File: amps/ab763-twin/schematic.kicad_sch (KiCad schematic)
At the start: 130 parts, among them T1 125P34A · 340-0-340 V, T2 125C1A, T3 125A29A, T4 125A20B

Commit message: Fix: schematic sheets — real title block, fitted paper, no lettering through circuitry
Every sheet in the corpus shipped with an EMPTY title block ("Title:" and
"Date:" blank, default "Sheet /" furniture) laid onto a fixed A4/A3 page
regardless of the drawing's size, with prose annotations placed by hand
wherever a coordinate looked free when the amp was first drawn. The result
read as an unfinished alpha under a `verified` badge: KiCanvas's default view
is `zoom_to_page()`, so a 150 x 110 mm circuit on an A3 sheet opened as a
postage stamp, and later edits had pushed live circuitry under the prose.

schematic_lib.py — the builder now records each element as a (kind, points,
extra) tuple instead of a finished string, so `write()` can measure and move
what it emits:

- emits a real `(title_block …)` read from the amp's own meta.yaml — Title =
  designation + style, Date = the verification (or added) date, Rev = the
  verification status, Company = Circuit Codex, plus the licence and source
  URL as comments. Fixes all 34 sheets from one place;
- emits `(paper "User" w h)` cut to the drawing, translated to a fixed margin,
  with the bottom 34 mm strip reserved for the worksheet's title block. Sheet
  utilisation of the drawable area went from as low as ~20% to 92-98%;
- `note()` queues prose into a wrapped band under the circuit, and `caption()`
  places a section heading over the block it names, nudging it clear if it
  would print through anything;
- per-symbol default label offsets (the old single default printed every pot's
  value through its own wiper arrow and every transformer's designator through
  its body), plus `place_labels()`, which moves any designator/value block that
  would print over ink;
- transformers and chokes are drawn, not boxed: iron core between two windings,
  centre taps where the part has them, and an optional `spec` lettering slot for
  a ratio or impedance;
- `gnd()` takes a direction, because a flag defaulting to "down" at the HEAD of
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
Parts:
- V1A, V1B, V2A, V2B, V4A, V4B: value 12AX7 -> 12AX7 (7025)
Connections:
- net B+2: no longer T4.2 (PRI_B)
- net at VRBV.3, VRMV.1, VRMV.2 (W): no longer CBV2.2
- net at VRBV.1, VRBV.2 (W), VRTV.3: no longer CBV.2
- net at VRBN.1, VRBN.2 (W), VRTN.3: no longer CBN.2
- net at VRBN.3, VRMN.1, VRMN.2 (W): no longer CBN2.2
- net at V3A.1 (P), V3B.1 (P): no longer T4.1 (PRI_P)
- net at CTO1.2, CTO3.2, V5B.2 (G): no longer VRSPD.1
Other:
- note removed: "AB763 (Twin Reverb) — Blackface Twin Reverb-style · Circuit Codex · CC-BY-SA 4.0 · redrawn from circuit facts"
- company: (none) -> Circuit Codex
- title: (none) -> AB763 (Twin) — Blackface Twin Reverb-style

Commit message: Fix: deterministic schematic ids and wires split at every join
- _u() is uuid5 over (amp id, emission order), so a regeneration of an
  unchanged script is byte-identical and a drift gate becomes possible
- write() splits wire segments at symbol pins, wire ends and junction dots,
  so the file connects exactly what the drawing shows under KiCad's
  endpoint-only semantics (270 pins were on a wire's interior; net
  partitions unchanged on all 38 sheets)
- all sheets regenerated; aa864-bassman title block was stale (draft) and
  now matches meta.yaml (verified)

Co-Authored-By: Claude Fable 5.1 <noreply@anthropic.com>
Claude-Session: https://claude.ai/code/session_01KBMfdh37HmCL2iWcBiL5J1
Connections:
- net GND: now also V9.1 (P)
- net at V8.1 (P): now also T3.1 (PRI_A), V7.1 (P)

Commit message: Fix: schematic wiring on ab763-twin, ab763, ab763-super
- long-tailed pair: the tail lead came off section B's PLATE pin; redrawn
  from its cathode on a joined-cathode lane under the bottle (all three)
- ab763-twin: V9/V10 plate run passed through V10's envelope and grounded
  cathode pin (one plate on ground, one floating); screen stubs 2 mm short
  of RSC1-4; V5B had no plate lead; driver grid bus through RGRD and CPIB
  riser through RFB1 (feedback node grounded); seven leads 4 mm short of
  their labels; VRBAL wiper carries -52 V per net_map
- ab763: same tail and RGRD faults; three pot ground flags 3.81 mm low;
  RNF2 had a wire ruled through its body
- ab763-super: V8 plate lead drawn from below its cathode; both reservoir
  bleeders shorted the supply to ground; RLV2 shorted by the stack output
  column; tremolo intensity feed ran through CTO1/VRSPD/RTO1 to ground;
  BP1 tap landed inside the choke body
- all three pass connectivity and verify_schematic_nets; no waivers

Co-Authored-By: Claude Fable 5.1 <noreply@anthropic.com>
Claude-Session: https://claude.ai/code/session_01KBMfdh37HmCL2iWcBiL5J1
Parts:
- removed CPIA: .001u, symbol cx:C
- removed RB2: 27k, symbol cx:R
- removed RBAL1, RBAL2: 220k 1W, symbol cx:R
- removed RD1: 1k 1W, symbol cx:R
- removed RD2: 4.7k 1W, symbol cx:R
- removed RFB2, RKE: 820, symbol cx:R
- removed RKRD: 2.2k, symbol cx:R
- removed RTO10: 10M, symbol cx:R
- removed V10, V7, V8, V9: 6L6GC, symbol cx:PENTODE
- removed V3A: 12AT7, symbol cx:TRIODE
- removed V5A: 12AX7, symbol cx:TRIODE
- added C10, C11: 70u 350V, symbol cx:C
- added C12, C13: 20u 525V, symbol cx:C
- added CKE, CKRD: 25u, symbol cx:C
- added OPTO: neon + photocell, symbol cx:OPTO
- added RGPA, RGRD: 1M, symbol cx:R
- added RLPA: 82k 5%, symbol cx:R
- added RSC1, RSC2, RSC3, RSC4: 470 1W, symbol cx:R
- added V5B: 12AX7, symbol cx:TRIODE
- added VRBAL: 10k-L bal, symbol cx:POT
- CPIA: renamed from RLPA; value 82k 5% -> .001u; symbol cx:R -> cx:C
- RB2: renamed from VRBAL; value 10k-L bal -> 27k; symbol cx:POT -> cx:R
- RBAL1: renamed from C10; value 70u 350V -> 220k 1W; symbol cx:C -> cx:R
- RBAL2: renamed from C11; value 70u 350V -> 220k 1W; symbol cx:C -> cx:R
- RD1: renamed from C12; value 20u 525V -> 1k 1W; symbol cx:C -> cx:R
- RD2: renamed from C13; value 20u 525V -> 4.7k 1W; symbol cx:C -> cx:R
- RFB2: renamed from RGPA; value 1M -> 820
- RKE: renamed from CKE; value 25u -> 820; symbol cx:C -> cx:R
- RKRD: renamed from CKRD; value 25u -> 2.2k; symbol cx:C -> cx:R
- RTO10: renamed from OPTO; value neon + photocell -> 10M; symbol cx:OPTO -> cx:R
- V10: renamed from RSC4; value 470 1W -> 6L6GC; symbol cx:R -> cx:PENTODE
- V3A: renamed from RGRD; value 1M -> 12AT7; symbol cx:R -> cx:TRIODE
- V7: renamed from RSC1; value 470 1W -> 6L6GC; symbol cx:R -> cx:PENTODE
- V8: renamed from RSC2; value 470 1W -> 6L6GC; symbol cx:R -> cx:PENTODE
- V9: renamed from RSC3; value 470 1W -> 6L6GC; symbol cx:R -> cx:PENTODE
- renumbered V5B to V5A
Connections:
- net -52V: now also VRBAL.2 (W)
- net B+1: now also C10.1
- net B+2: now also RTO10.2, C12.1, RSC1.2, RSC2.2, RSC3.2, RSC4.2; no longer V10.2, V7.2, V8.2, V9.2
- net B+3: now also RD1.2, C13.1, RLPA.1; no longer CPIA.1
- net B+4: now also RD2.2
- net BIAS TAP: now also RBIAS.1
- net GND: now also RB2.2, V10.4 (K), V7.4 (K), V8.4 (K), V9.4 (K), C11.2, C12.2, C13.2, CKE.2, CKRD.2, RGRD.2; no longer CPIB.1, CRS.1, RD1.2, RD2.2, RFB1.1, RT22.1, T3.3 (PRI_B), V3A.1, V3A.2, V3B.2 (G)
- net MAINS: now also CDEATH.1
- net MIXER: now also CPIA.1
- net MIXG: now also CRS.2, OPTO.3 (P1); no longer RTO10.3 (P1)
- net NORM 1: now also R1n.1
- net NORM 2: now also R2n.1
- net SPKR: now also RFB2.1
- net TANK RET: now also RGR1.1
- net VIB 1: now also R1v.1
- net VIB 2: now also R2v.1
- net at CTO3.1, RTO1.2: now also V5A.1 (P)
- net at CTO2.1, RTOG1.1, RTOG2.2: now also V5A.2 (G)
- net at CKTO1.1, RKTO1.1: now also V5A.3 (K)
- net at RTO10.1: now also OPTO.1 (L1), V5B.1 (P)
- net at RLAMP.2: now also OPTO.2 (L2); no longer RTO10.2 (L2)
- net at VRINT.1: now also VRINT.2 (W), OPTO.4 (P2); no longer RTO10.4 (P2)
- net at RKRD.1, V3B.3 (K): now also V3A.3 (K), CKRD.1
- net at RST4.2: now also V10.2 (G1)
- net at CTO1.2, CTO3.2: now also VRSPD.1, VRSPD.2 (W), V5B.2 (G); no longer V5A.2 (G)
- net at T3.1 (PRI_A): now also V7.1 (P), V8.1 (P)
- net at RST2.2: now also V8.2 (G1)
- net at RST1.2: now also V7.2 (G1)
- net at C1.1, V6A.1 (P): now also RLPA.2; no longer CPIA.2
- net at V6A.2 (G): now also CPIA.2, RGPA.1; no longer RFB2.1
- net at C2.1, RLPB.2, V6B.1 (P): no longer RTAIL.2, V6A.3 (K)
- net at CB1.1, DBIAS.2 (K): now also VRBAL.1; no longer RB2.1
- net at CKTO2.1, RKTO2.1: now also V5B.3 (K); no longer V5A.3 (K)
- net at V3B.1 (P): now also V3A.1 (P)
- net at RBAL1.2, RBAL2.1: now also C10.2, C11.1
- net at RKE.1, V4A.3 (K), V4B.3 (K): now also CKE.1
- net at V10.1 (P): now also T3.3 (PRI_B), V9.1 (P)
- net at RST3.2: now also V9.2 (G1)
- net at RGPB.1, RT22.2, RTAIL.1: now also RGPA.2; no longer RFB2.2
- net at V6B.3 (K): now also RTAIL.2, V6A.3 (K)
- new net: CRS.1, RGRD.1, V3A.2 (G), V3B.2 (G)
- new net: RB2.1, VRBAL.3
- new net: RSC2.1, V8.3 (G2)
- new net: RSC4.1, V10.3 (G2)
- new net: RSC1.1, V7.3 (G2)
- new net: CPIB.1, RFB1.1, RFB2.2, RT22.1
- new net: RSC3.1, V9.3 (G2)
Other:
- moved on the sheet: RFB2, V5A, VRSPD

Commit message: Add: real tube pin numbers and readable valve glyphs on every schematic
Phase B of the drawing program. A factory service sheet numbers every tube
pin, because the number is what a technician puts a probe on. This corpus
printed none, and the numbers hidden in its symbols were positional
placeholders (P=1, G=2, K=3) that would have published a 6V6GT's plate as
pin 1 when it is pin 3.

1055 electrodes now carry the real number, 1027 lettered (27 are shared
filaments deduped, 1 dropped for want of clear space on the 6G2). Resolved per
instance from reference/tubes/<slug>.yaml through the same alias resolution the
layout renderer uses, so a 12AX7 section and a 6SL7 section each get their own
basing. A valve whose basing the corpus does not carry prints nothing rather
than a wrong number.

Section letters and basing units are now separate things, which cost a detour
worth recording. The RCA 12AX7-A sheet reads "Pin 1 - Plate of Unit No.2 ...
Pin 6 - Plate of Unit No.1", so unit numbering is not pin order; the 5Y3 and
GZ34 number their units in opposite pin order, so nothing positional can
express it. But the section LETTER is a designator, not a basing fact: this
corpus, like every technician, calls the first stage in signal order V1A, and
five amps' prose already did. On four amps the factory sheets put that first
stage on the other half -- the AA764's own schematic prints +200 V on pin 1 --
so those drawings now state their unit explicitly, each citing its source, and
no letter, netlist, parts list or layout comment changed. 183 layout comments
agree with the printed numbers, 0 disagree. A guard fires if two halves of one
bottle resolve to the same unit, which is exactly how this was found.

Glyphs: the cathode gains a bracket and filament hairpin so it can no longer be
confused with the plate bar, the pentode's screen sits on its own row, and a
rectifier draws as one envelope over its sections instead of two apparent
bottles. Line weights are scaled per sheet to a co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
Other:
- note added: "1"
- note added: "2"
- note added: "3"
- note added: "4"
- note added: "5"
- note added: "6"
- note added: "7"
- note added: "8"

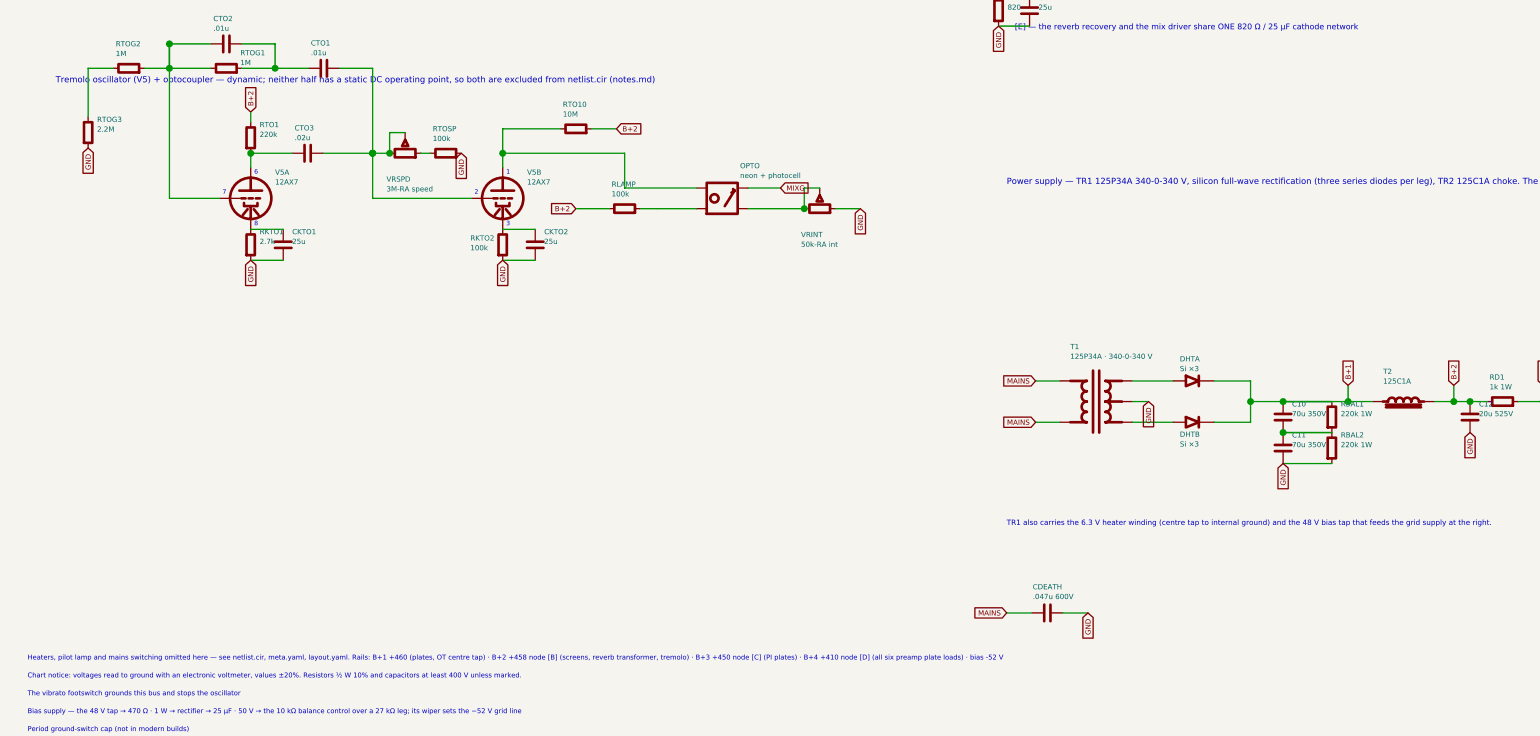
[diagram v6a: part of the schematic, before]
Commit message: Fix: schematic sheet notes no longer name repository files
Thirty-seven committed sheets rendered footnotes and section notes such as
"Heaters and PT primary omitted — see netlist.cir and meta.yaml" or
"excluded from netlist.cir (notes.md)" to visitors through KiCanvas. The
prose sweeps never counted sheets. Rewritten in the site's own words — the
netlist, the sources list, the circuit story, the parts list, the board
drawing — in 59 strings across 33 draw scripts, keeping every technical
claim as it was; the three tone sheets (6G4, 6G5, 6G6-B) are under repair
elsewhere and keep theirs for now. The sweep touched only strings passed to
the sheet's note, text, caption and footnote calls, never a path or a value.

Gates: check_schematics 40/0, connectivity 0 isolated pins;
verify_schematic_nets 40 clean; only the regenerated sheets and their served
copies changed.

Co-Authored-By: Claude Fable 5.1 <noreply@anthropic.com>
Claude-Session: https://claude.ai/code/session_01KBMfdh37HmCL2iWcBiL5J1
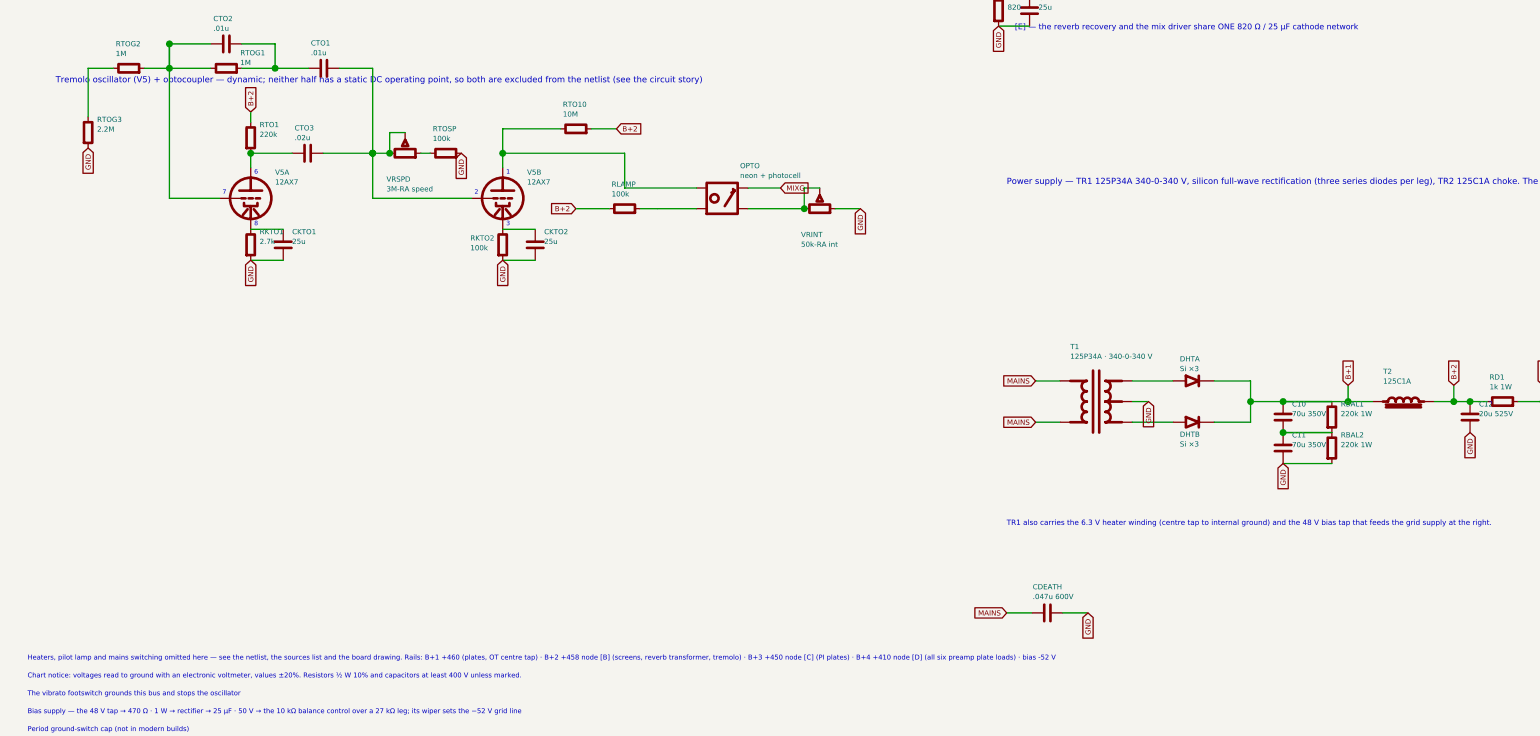
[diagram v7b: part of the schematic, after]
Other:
- note added: "Heaters, pilot lamp and mains switching omitted here — see the netlist, the sources list and the board drawing. Rails: B+1 +460 (plates, OT centre tap) · B+2 +458 node [B] (screens, reverb transformer, tremolo) · B+3 +450 node [C] (PI plates) · B+4 +410 node [D] (all six preamp plate loads) · bias -52 V"
- note added: "Tremolo oscillator (V5) + optocoupler — dynamic; neither half has a static DC operating point, so both are excluded from the netlist (see the circuit story)"
- note removed: "Heaters, pilot lamp and mains switching omitted here — see netlist.cir, meta.yaml, layout.yaml. Rails: B+1 +460 (plates, OT centre tap) · B+2 +458 node [B] (screens, reverb transformer, tremolo) · B+3 +450 node [C] (PI plates) · B+4 +410 node [D] (all six preamp plate loads) · bias -52 V"
- note removed: "Tremolo oscillator (V5) + optocoupler — dynamic; neither half has a static DC operating point, so both are excluded from netlist.cir (notes.md)"
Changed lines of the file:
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@@
     (stroke (width 0) (type default)))
   (junction (at 259.229 225.889) (diameter 1.7) (color 0 0 0 0))
-  (text "Tremolo oscillator (V5) + optocoupler — dynamic; neither half has a static DC operating point, so both are excluded from netlist.cir (notes.md)" (at 19.6088 246.889 0)
+  (text "Tremolo oscillator (V5) + optocoupler — dynamic; neither half has a static DC operating point, so both are excluded from the netlist (see the circuit story)" (at 19.6088 246.889 0)
     (effects (font (size 1.5 1.5)) (justify left)))
   (symbol (lib_id "cx:TRIODE") (at 67.6088 275.889 0) (unit 1)
@@
   (text "8" (at 416.459 181.604 0)
     (effects (font (size 1.1 1.1)) (justify left)))
-  (text "Heaters, pilot lamp and mains switching omitted here — see netlist.cir, meta.yaml, layout.yaml. Rails: B+1 +460 (plates, OT centre tap) · B+2 +458 node [B] (screens, reverb transformer, tremolo) · B+3 +450 node [C] (PI plates) · B+4 +410 node [D] (all six preamp plate loads) · bias -52 V" (at 12.7 389.047 0)
+  (text "Heaters, pilot lamp and mains switching omitted here — see the netlist, the sources list and the board drawing. Rails: B+1 +460 (plates, OT centre tap) · B+2 +458 node [B] (screens, reverb transformer, tremolo) · B+3 +450 node [C] (PI plates) · B+4 +410 node [D] (all six preamp plate loads) · bias -52 V" (at 12.7 389.047 0)
     (effects (font (size 1.2 1.2)) (justify left)))
   (text "Chart notice: voltages read to ground with an electronic voltmeter, values ±20%. Resistors ½ W 10% and capacitors at least 400 V unless marked." (at 12.7 393.447 0)
